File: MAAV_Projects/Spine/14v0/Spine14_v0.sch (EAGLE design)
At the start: 123 parts, among them IC3 PINTO_SMD, J7 MA04-1, Q1 MOSFET-NCHANNELBSS138, Q10 BSS138, Q11 BSS138, Q12 BSS138, Q13 BSS138, Q14 BSS138, Q2 BSS138, Q3 MOSFET-NCHANNELBSS138, Q4 MOSFET-NCHANNELBSS138, Q5 32.768KHz, Q6 16MHz, Q7 CRYSTAL_16MHZ_SMD, Q8 MOSFET-NCHANNELBSS138, Q9 MOSFET-NCHANNELBSS138, U1 ATMEGA328-AU, U2 REG_3V_8SOIC

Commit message: changed motor output to 3v3 logic. going to add switches, SD card, and IMU, then i should be finished with schematic
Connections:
- net MOTOR0_PWM_5V renamed MOTOR0_PWM_3V3
- net MOTOR1_PWM_5V renamed MOTOR1_PWM_3V3
- net MOTOR2_PWM_5V renamed MOTOR2_PWM_3V3
- net MOTOR3_PWM_5V renamed MOTOR3_PWM_3V3
- net +3V3: now also JP0.P$2, JP1.P$2, JP2.P$2, JP3.P$2, R10.1, R26.1, R28.1, R6.1
- net +5V: no longer JP0.P$2, JP1.P$2, JP2.P$2, JP3.P$2, R10.1, R26.1, R28.1, R6.1

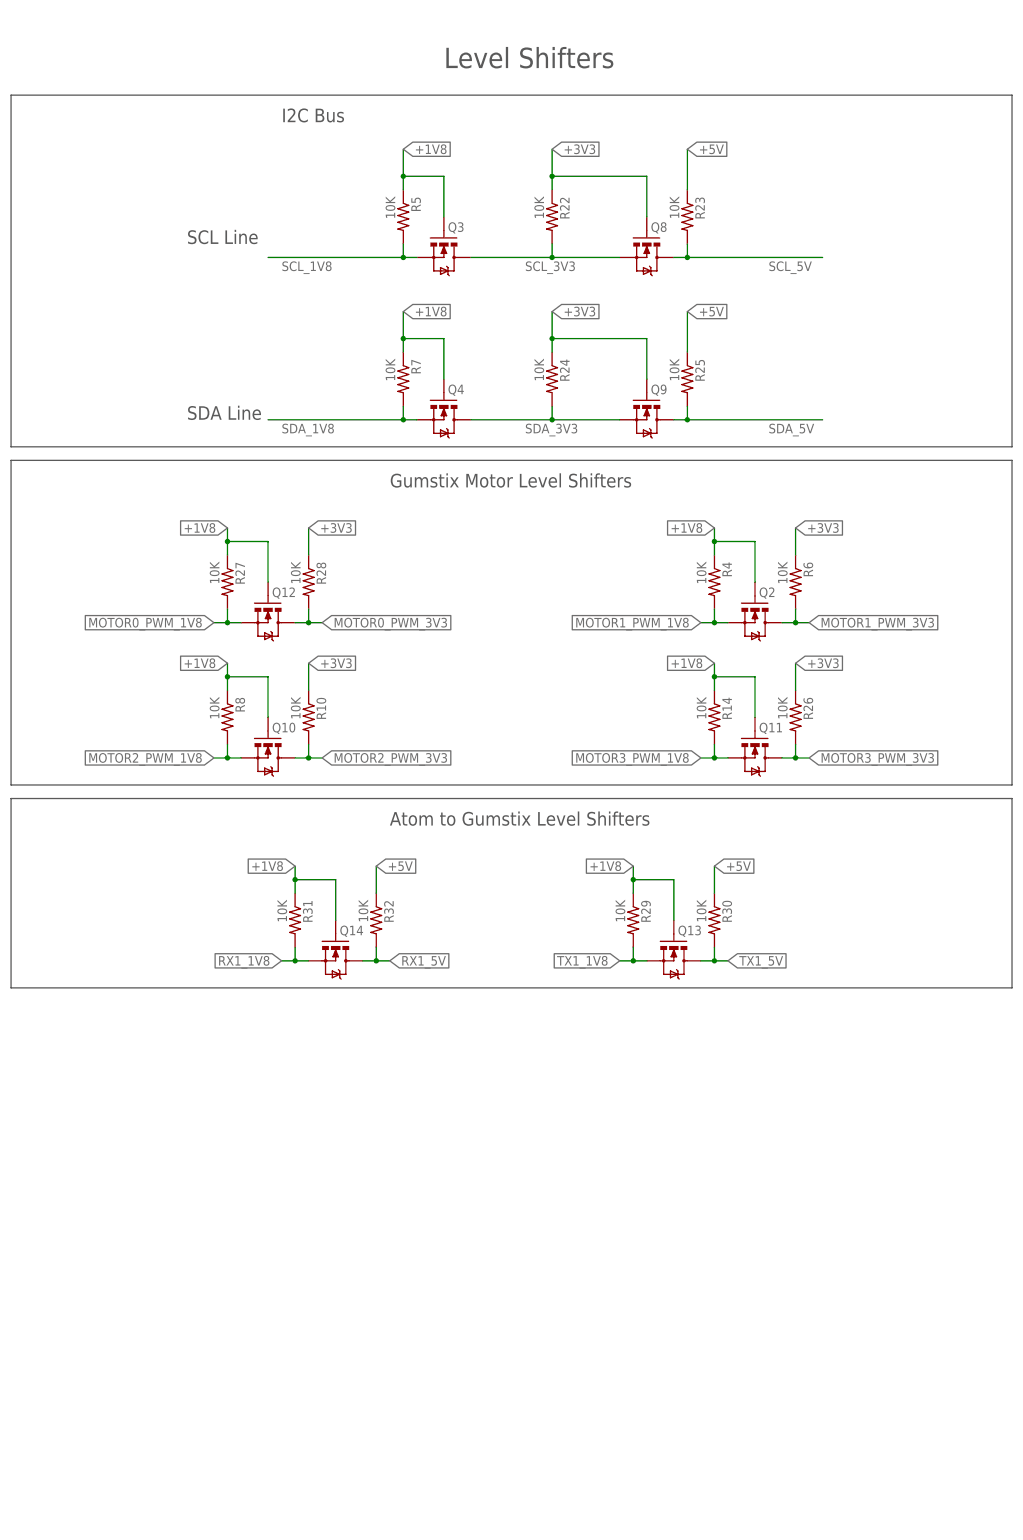
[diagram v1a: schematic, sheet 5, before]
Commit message: just need to add switches and IMU and should be done with all the essentials... time to move on to the KNIGHT RIDERRRR. also working on a 4PDT switch
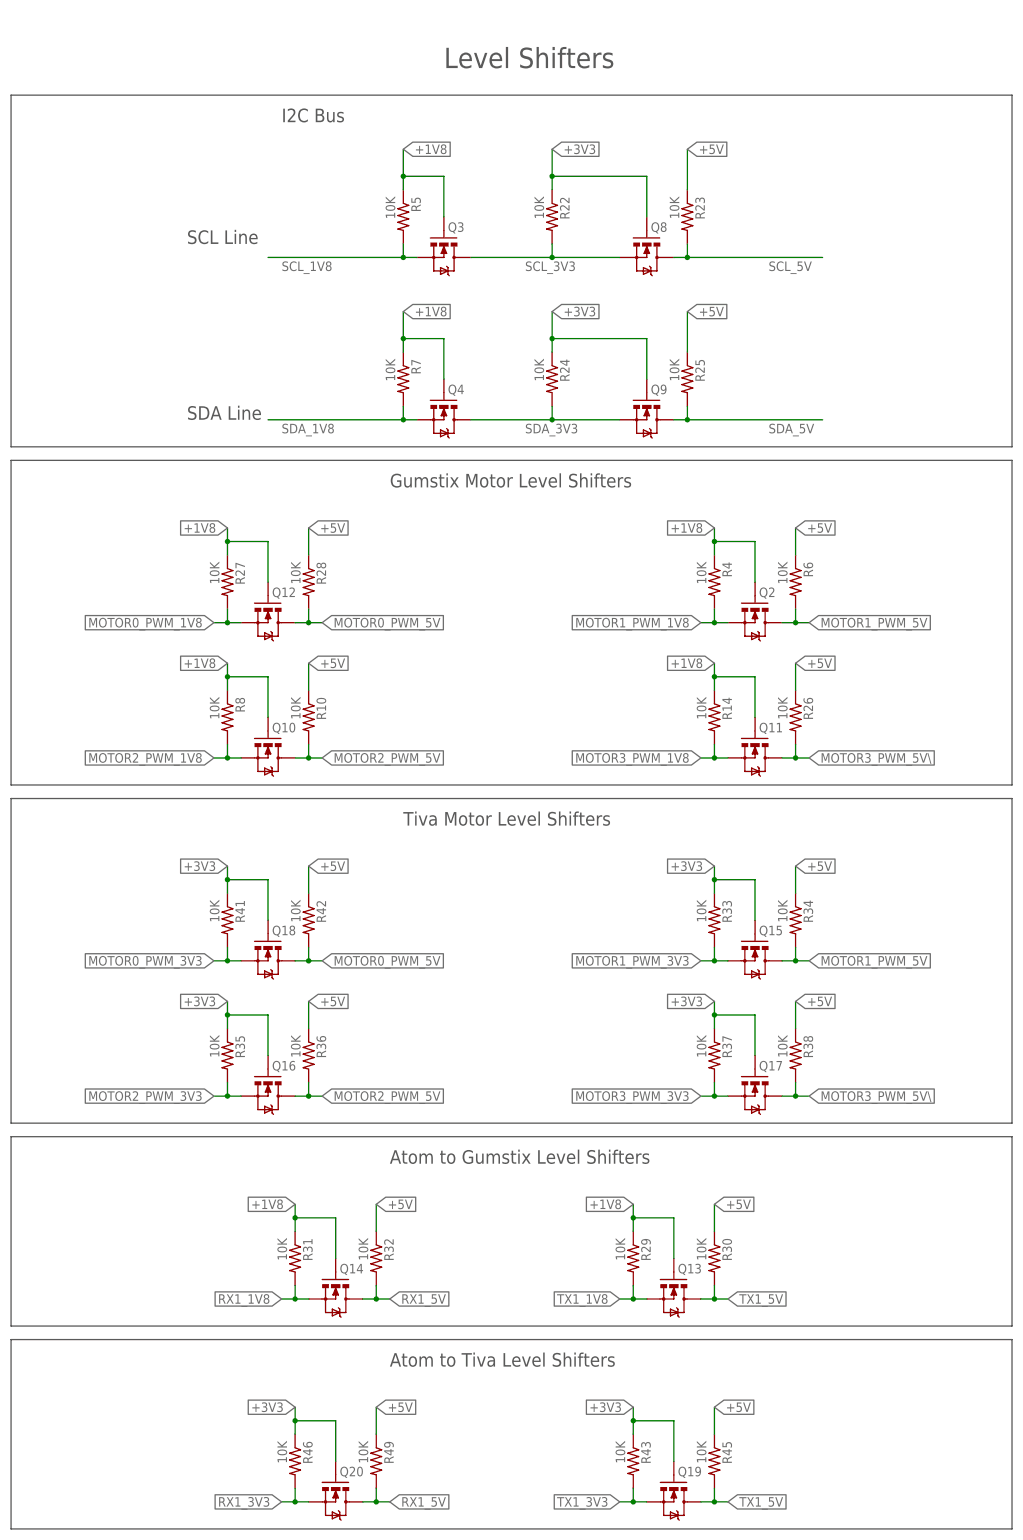
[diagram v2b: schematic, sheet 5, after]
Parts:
- added C26: 2.2uF, rcl:C-USC0805
- added C27: 330uF, rcl:CPOL-USF
- added Q15, Q16, Q17, Q18, Q19, Q20: BSS138, SparkFun-DiscreteSemi:MOSFET-NCHANNELBSS138
- added R33, R34, R35, R36, R37, R38, R41, R42, R43, R45, R46, R49: 10K, SparkFun:RESISTOR0603-RES
- added RSET: 21.0k, rcl:R-US_R0805
- added U$5: POWER-MODULE-TI-6A_SOLDERLESS_TERMINAL, MAAV:POWER-MODULE-TI-6A_SOLDERLESS_TERMINAL
- added V_BATT1: BATT-CONN-50A_MINI-FIT-SR_THRU-HOLE, MAAV:BATT-CONN-50A_MINI-FIT-SR_THRU-HOLE
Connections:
- new net MOTOR0_PWM_5V: JP0.P$1, Q12.D, Q18.D, R28.2, R42.2
- new net MOTOR1_PWM_5V: JP1.P$1, Q15.D, Q2.D, R34.2, R6.2
- new net MOTOR2_PWM_5V: JP2.P$1, Q10.D, Q16.D, R10.2, R36.2
- new net MOTOR3_PWM_5V: JP3.P$1
- new net MOTOR3_PWM_5V\: Q11.D, Q17.D, R26.2, R38.2
- new net N$18: RSET.1, U$5.ADJ
- new net N$20: C26.1, U$5.V_I, V_BATT1.VCC
- new net RX1_3V3: Q20.S, R46.2
- new net TX1_3V3: Q19.S, R43.2
- net +3V3: now also Q15.G, Q16.G, Q17.G, Q18.G, Q19.G, Q20.G, R33.1, R35.1, R37.1, R41.1, R43.1, R46.1; no longer JP0.P$2, JP1.P$2, JP2.P$2, JP3.P$2, R10.1, R26.1, R28.1, R6.1
- net +5V: now also C27.+, JP0.P$2, JP1.P$2, JP2.P$2, JP3.P$2, R10.1, R26.1, R28.1, R34.1, R36.1, R38.1, R42.1, R45.1, R49.1, R6.1, U$5.SENSE, U$5.V_O
- net GND: now also C26.2, C27.-, RSET.2, U$5.GND@0, U$5.GND@1, V_BATT1.GND
- net MOTOR0_PWM_3V3: now also Q18.S, R41.2; no longer JP0.P$1, Q12.D, R28.2
- net MOTOR1_PWM_3V3: now also Q15.S, R33.2; no longer JP1.P$1, Q2.D, R6.2
- net MOTOR2_PWM_3V3: now also Q16.S, R35.2; no longer JP2.P$1, Q10.D, R10.2
- net MOTOR3_PWM_3V3: now also Q17.S, R37.2; no longer JP3.P$1, Q11.D, R26.2
- net ON/OFF: now also U$5.INHIBIT
- net RX1_5V: now also Q20.D, R49.2
- net TX1_5V: now also Q19.D, R45.2
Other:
- note added: "Atom to Tiva Level Shifters"
- note added: "Tiva Motor Level Shifters"
- moved on the sheet: Q13, Q14, R29, R30, R31, R32
